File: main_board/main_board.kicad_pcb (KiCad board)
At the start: 2 copper layers, 35 x 47.5 mm, 14 parts, among them SW1 SW_Push, SW2 SW_Push, U1 XIAO ESP32C3

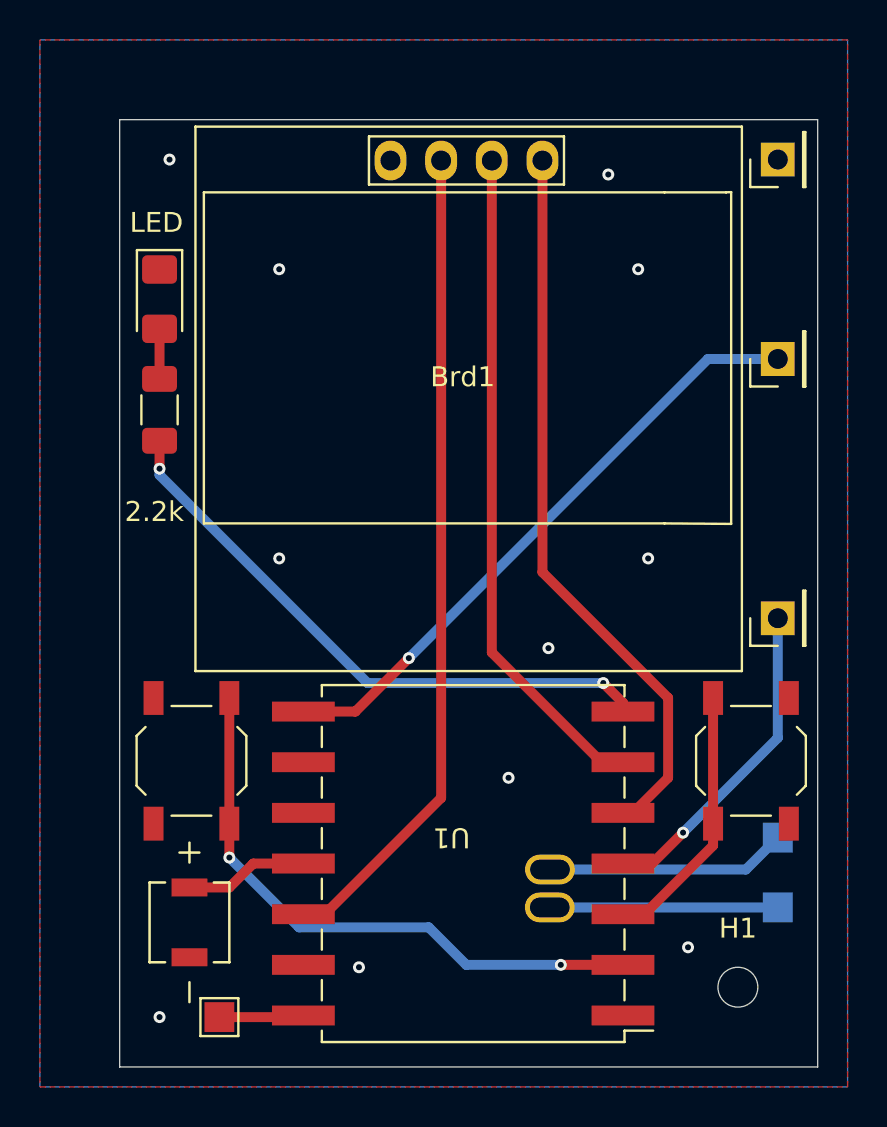
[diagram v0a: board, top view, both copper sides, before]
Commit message: I updated the case in the hardware folder
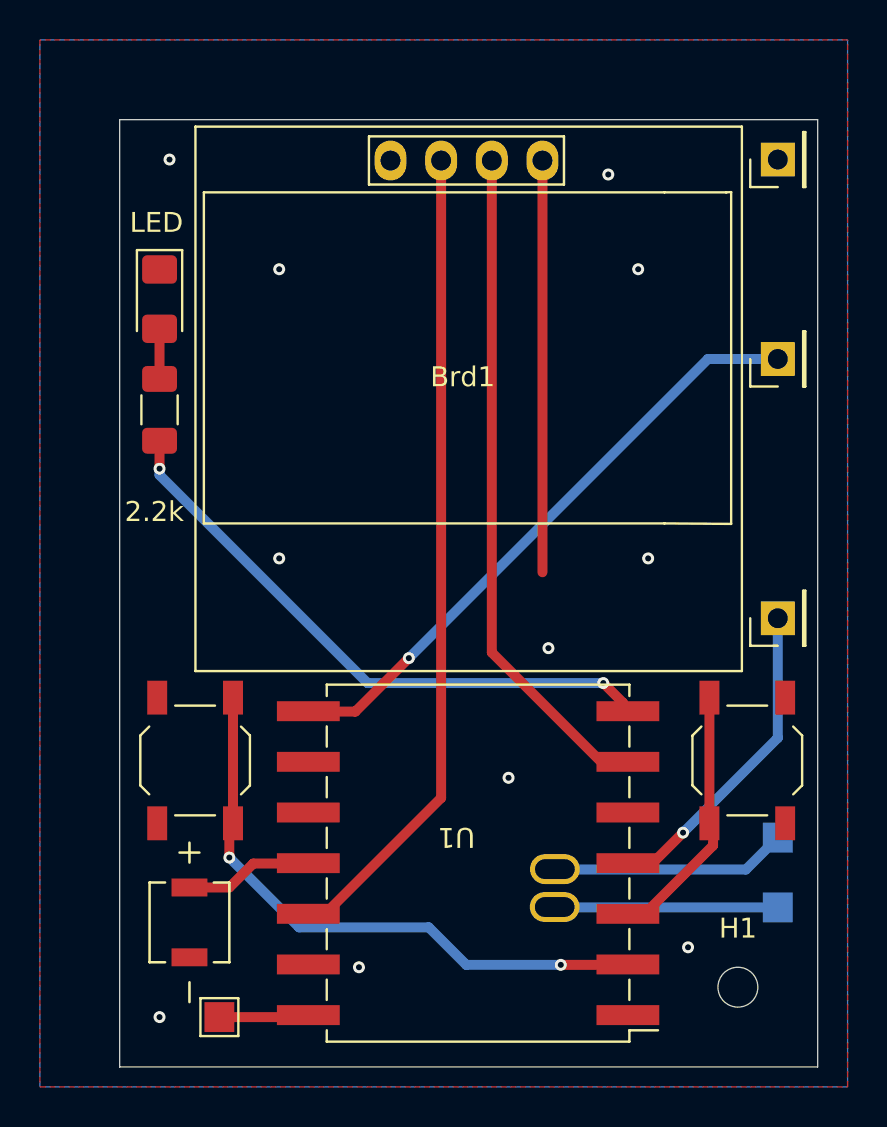
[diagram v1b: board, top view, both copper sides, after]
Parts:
- moved U1 0.25 mm to (105.4, 95.0)
- moved SW2 0.19 mm to (120.0, 91.6)
- moved SW1 0.18 mm to (92.3, 91.6)
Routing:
- net Net-(Brd1-SDA): track 36.6 -> 20.9 mm
- net Net-(U1-D3): track 16.6 -> 16.1 mm
